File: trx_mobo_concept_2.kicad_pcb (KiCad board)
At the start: 2 copper layers, 200 x 100 mm, 416 parts, among them J301 CONN_SMA_VERT, J302 CONN2, J303 CONN_SMA_VERT, J304 CONN3, J305 CONN_SMA_VERT, J306 CONN3, J307 CONN2, J308 CONN_SMA_VERT, J309 CONN8, Q1201 BSS138, Q1301 MMBT3904, Q1302 MMBT3904, Q1303 MMBT3904, Q1601 SI2369, Q1602 BSS138, Q1603 MMBT3904, Q1604 SI2369, Q1605 BSS138, Q1606 MMBT3904, Q1701 MMBT3906, Q1702 MMBT3904, Q1703 MMBT3904, Q2101 2SC3357, Q2102 2SC3357, Q2301 2SC3357, Q301 BSS138, Q401 BSS138, Q402 BSS138, Q801 MMBT3904, Q901 MMBFJ310, Q902 MMBFJ310, Q903 MMBT3904, Q904 MMBT3904, Q905 BSS138, T2101 XFMR_RF_BIFILAR, T2102 XFMR_RF_BIFILAR, T2301 XFMR_RF_BIFILAR, T801 XFMR_RF_BIFILAR, T901 FT37-43, U1101 DG449DS-T1-E3, U1102 LMC6482, U1103 LMC6482, U1201 LM380N, U1301 ADE-1, U1701 LMC6482, U1801 AS169-73, U1802 AS169-73, U2101 AS169-73, U2102 AS169-73, U2201 ADE-1, U2301 AS169-73, U2302 AS169-73, U401 24CW640, U402 MCP4725, U403 74LVC1G00, U501 PCA9554APW, U801 ADE-1, Y2001 45.1 MHz, Y2002 45.1 MHz, Y701 12.288 MHz, Y702 12.288 MHz, Y703 12.288 MHz, Y704 12.288 MHz, Y705 12.288 MHz, Y706 12.288 MHz

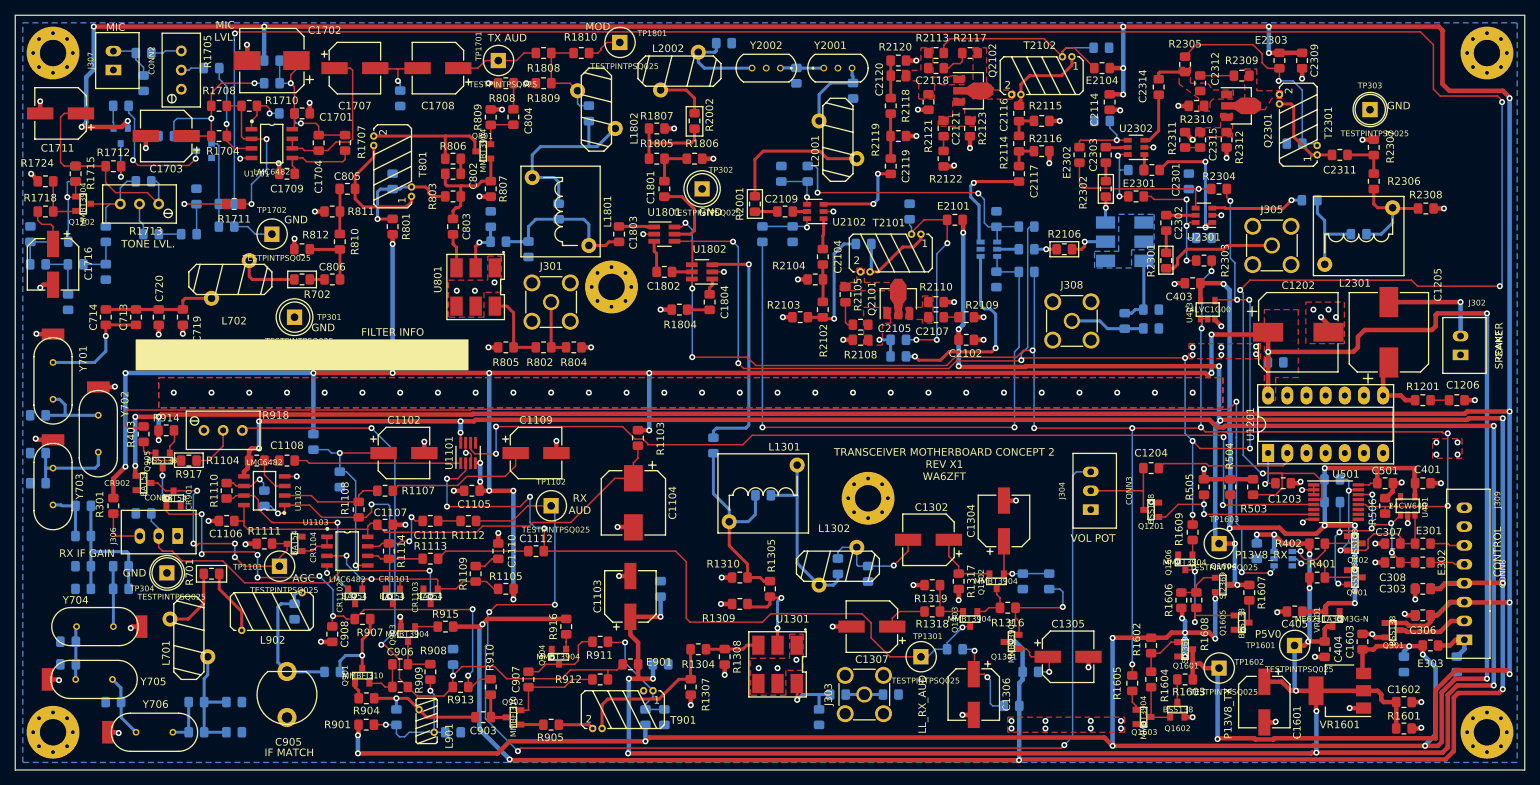
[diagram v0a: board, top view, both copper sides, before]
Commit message: Update pcb database to version 6
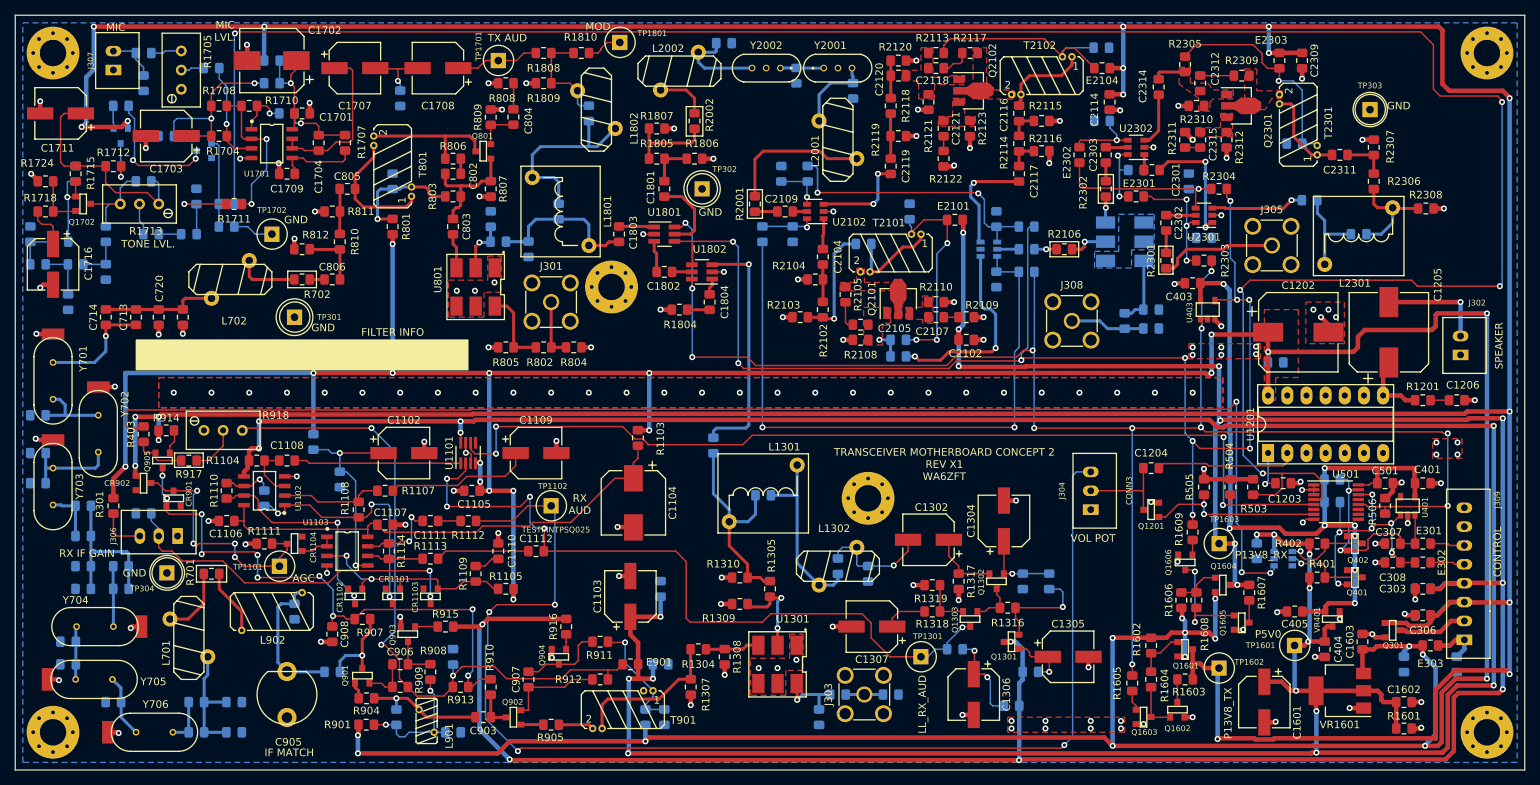
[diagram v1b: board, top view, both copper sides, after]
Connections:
- net /top/connectors/~TX renamed /top/connectors/~{TX}
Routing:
- net /top/ENA_TUNE_OSC_3V3: track 303.9 -> 301.3 mm
- net /top/PTT_3V3_N: track 176.9 -> 176.2 mm
- net Net-(C908-Pad1): track 76.4 -> 75.8 mm
- net /top/radio/prod_det_tx_mix/agc/APBIAS: track 28.0 -> 27.4 mm
- net Net-(C2118-Pad1): track 4.56 -> 3.94 mm
- net Net-(C2101-Pad1): track 28.9 -> 28.3 mm
- net /top/P13V8: vias 31 -> 30
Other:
- net class Default removed
- net class Power removed
- net class RF removed

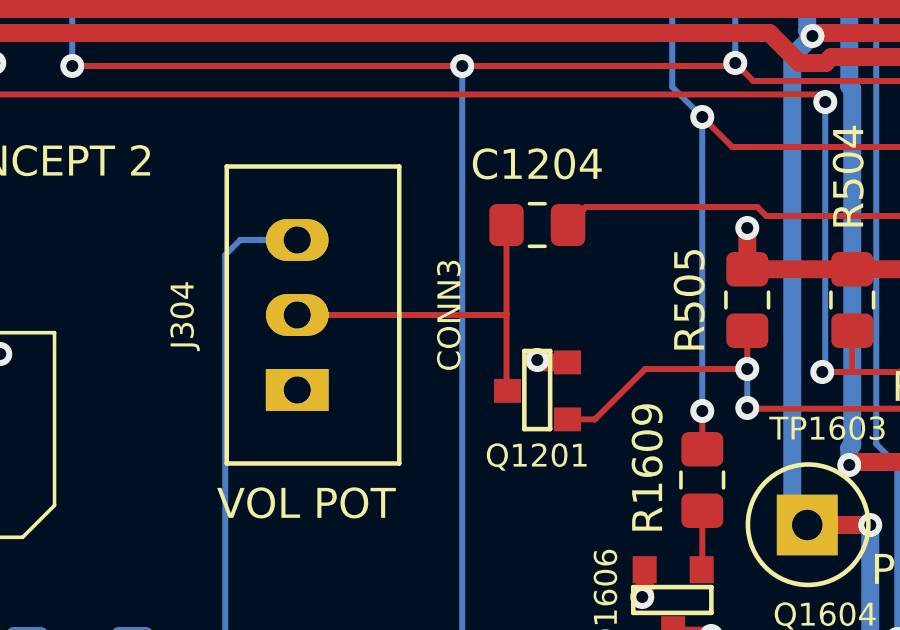
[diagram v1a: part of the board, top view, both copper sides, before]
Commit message: Sync PCB with schematic
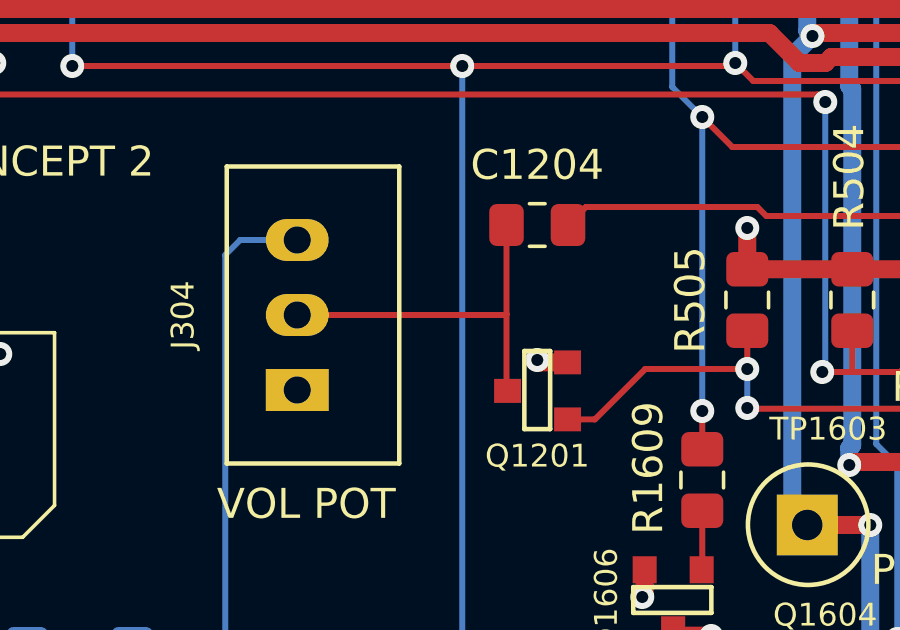
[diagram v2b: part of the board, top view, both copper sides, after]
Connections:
- net /top/i2c/MUTE_RX_AUDIO renamed /top/radio/MUTE_RX_AUDIO
- net /top/radio/prod_det_tx_mix/IF_IN_12R288 renamed /top/radio/ifagc/IF_OUT
- net /top/radio/rf_45r1_mic_amp_tune_osc/TX_IF_IN_45R1 renamed /top/radio/prod_det_tx_mix/TX_IF_OUT_45R1
- net /top/radio/rf_45r1_mic_amp_tune_osc/if_45r1_mic_amp_tune_osc/trx_switch/AUDIO_IN renamed /top/radio/rf_45r1_mic_amp_tune_osc/if_45r1_mic_amp_tune_osc/speech_amp/AUDIO_OUT
- net /top/radio/rf_45r1_mic_amp_tune_osc/transverter/bd_amp_45R1/BDA_LEFT renamed /top/radio/rf_45r1_mic_amp_tune_osc/transverter/THIRD_MIXER/IF
- U1101 pad 5: (no net) -> unconnected-(U1101-Pad5)
- U1201 pad 13: (no net) -> unconnected-(U1201-Pad13)
- U1201 pad 6: (no net) -> unconnected-(U1201-Pad6)
- U1201 pad 9: (no net) -> unconnected-(U1201-Pad9)
- U401 pad 5: (no net) -> unconnected-(U401-Pad5)
- U501 pad 10: (no net) -> unconnected-(U501-Pad10)
- U501 pad 11: (no net) -> unconnected-(U501-Pad11)
- U501 pad 13: (no net) -> unconnected-(U501-Pad13)
- U501 pad 6: (no net) -> unconnected-(U501-Pad6)
- U501 pad 9: (no net) -> unconnected-(U501-Pad9)

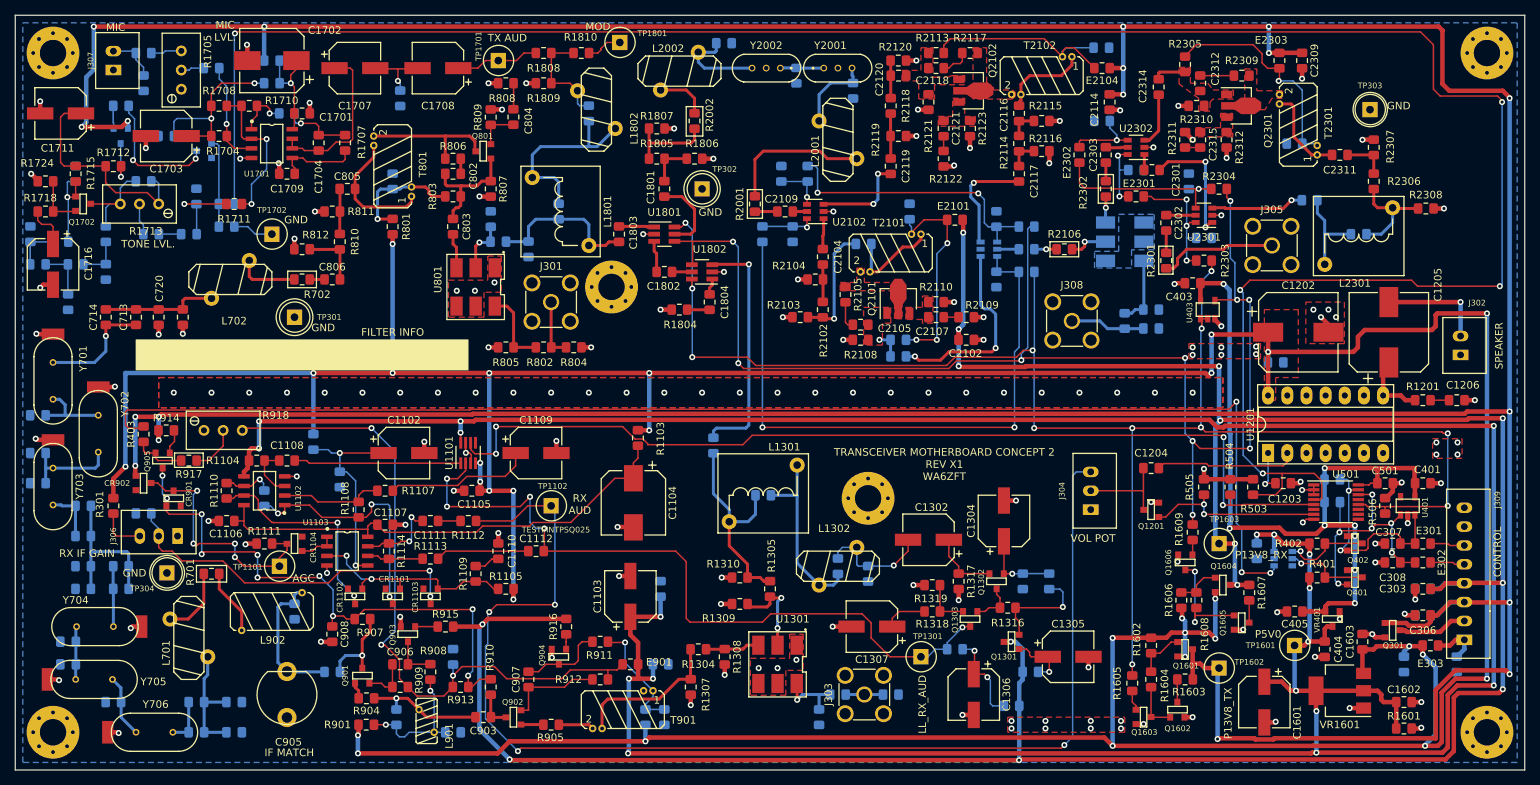
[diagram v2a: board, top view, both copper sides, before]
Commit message: Fix BOM part number errors and out of sync footprints which happened during conversion from Kicad 5 to 6
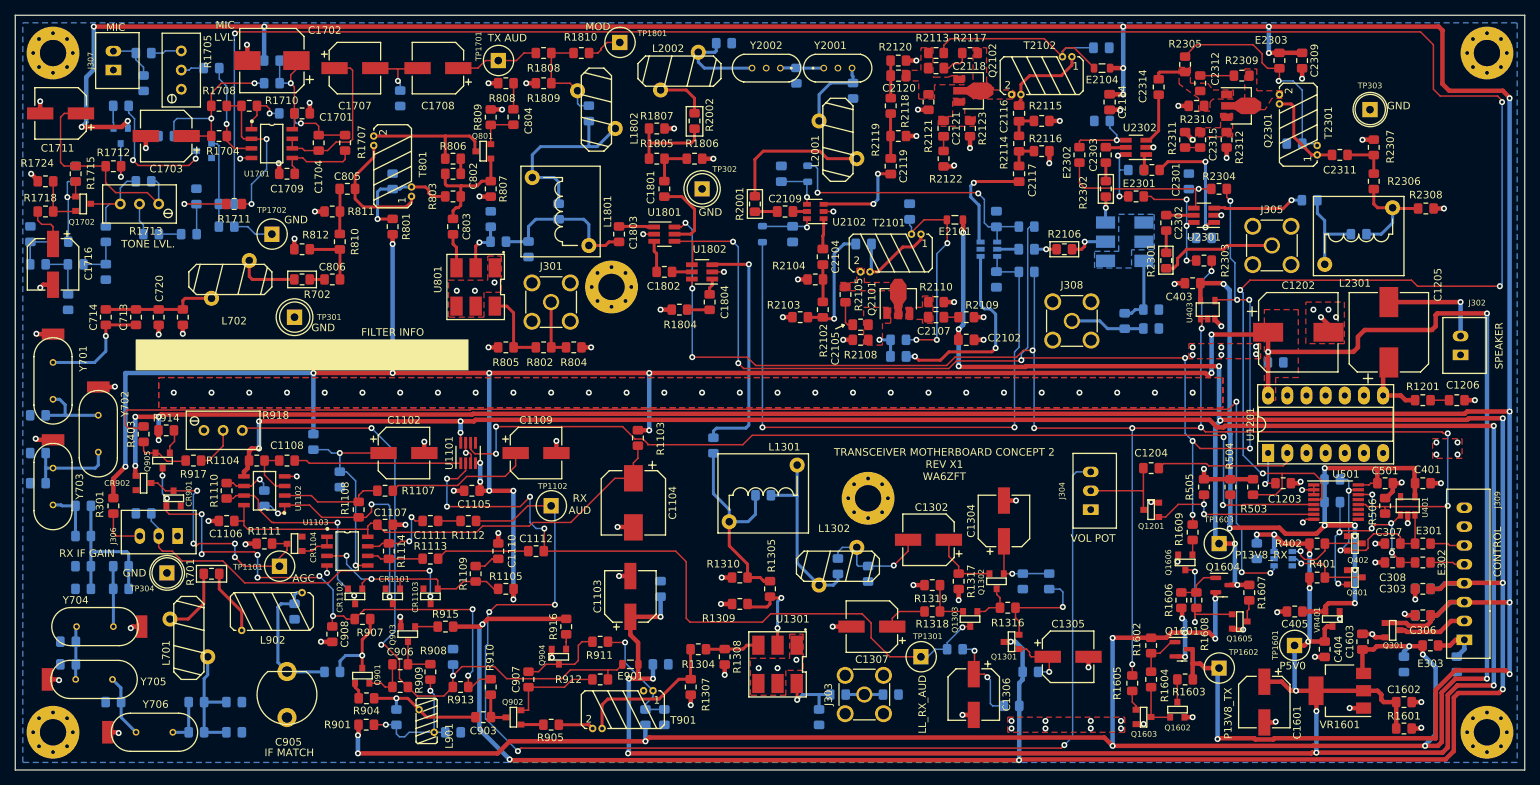
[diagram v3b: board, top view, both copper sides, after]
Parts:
- C1603, C2101, C2102, C2103, C2104, C2105, C2106, C2107, C2108, C2109, C2110, C2111, C2112, C2113, C2114, C2115, C2116, C2117, C2118, C2119, C2120, C2121: footprint Capacitor_SMD:C_0805_2012Metric_Pad1.15x1.40mm_HandSolder -> Capacitor_SMD:C_0805_2012Metric_Pad1.18x1.45mm_HandSolder
- C2002: value 8.2p -> 13p
- E2101, E2102, E2103, E2104, E901: footprint Inductor_SMD:L_0805_2012Metric_Pad1.15x1.40mm_HandSolder -> Inductor_SMD:L_0805_2012Metric
- Q1601, Q1604: footprint mods:SOT23-3-SAR -> Package_TO_SOT_SMD:SOT-23
- R1114: value 47K -> 10K
- R2309: value 1.6K -> 330
- R2311: value 6.8 -> 22
- R803: value 3.9K -> 8.2K
- R807: value 750 -> 1.5K
- R809: value 30 -> 120
- U2301, U2302: footprint Package_TO_SOT_SMD:SOT-23-6 -> Package_TO_SOT_SMD:SOT-23-6_Handsoldering
- moved R917 0.60 mm to (73.6, 109.0)
- moved Q1601 0.41 mm to (204.6, 134.0), turned to 0 degrees
- moved Q1605 0.29 mm to (212.2, 130.3)
- turned Q1604 to 0 degrees
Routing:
- net Net-(R917-Pad1): track 6.38 -> 5.78 mm
